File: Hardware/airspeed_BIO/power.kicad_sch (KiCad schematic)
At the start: 13 parts, among them Q1 2N7002, U1 MP2637GR-P

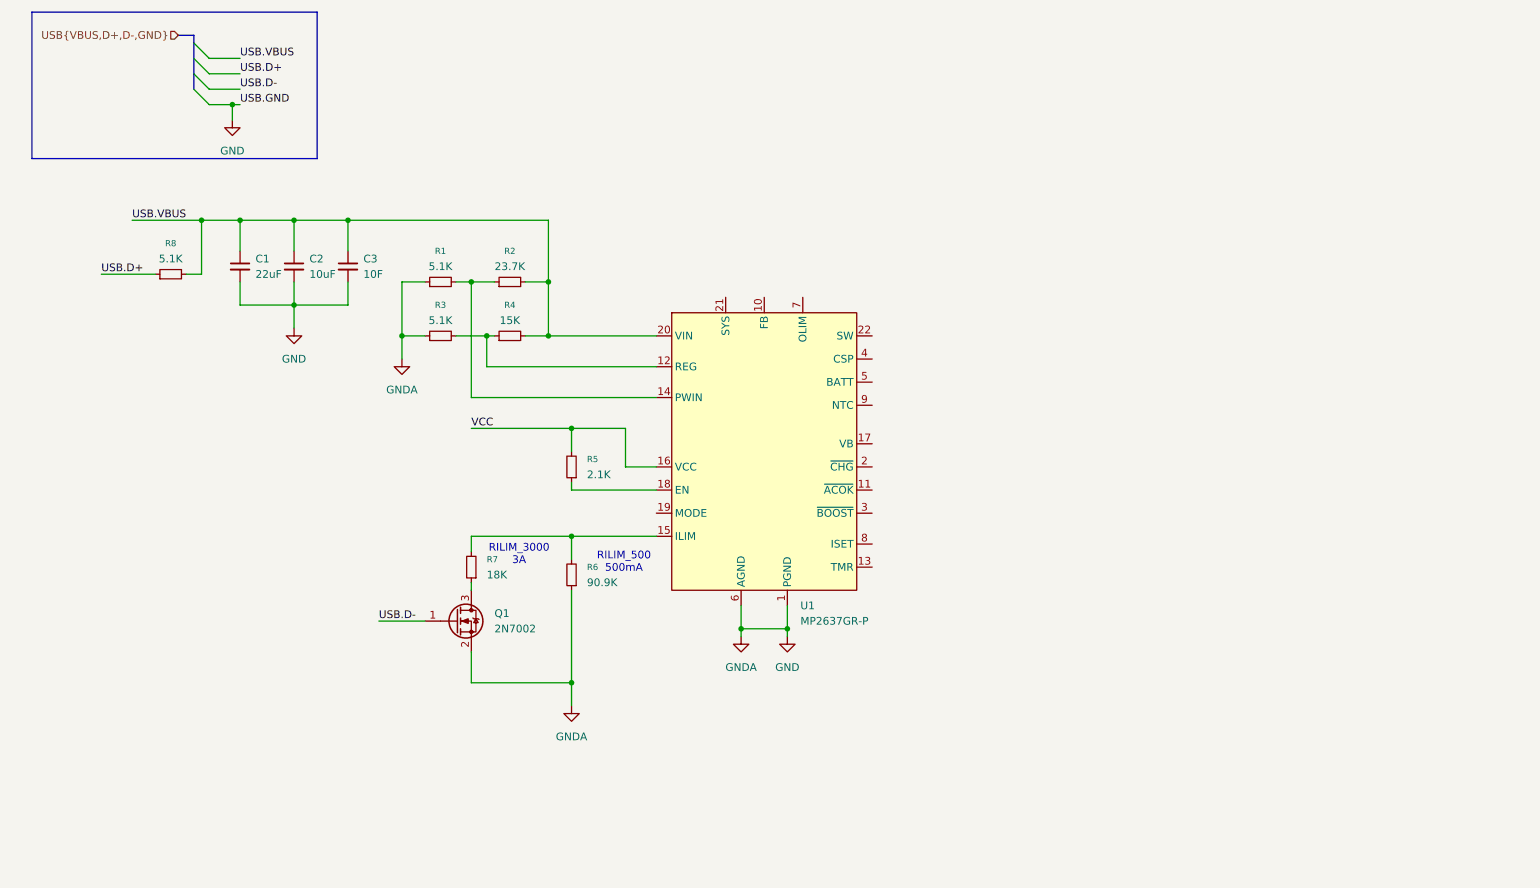
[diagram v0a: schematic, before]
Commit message: power end didn't set I limit
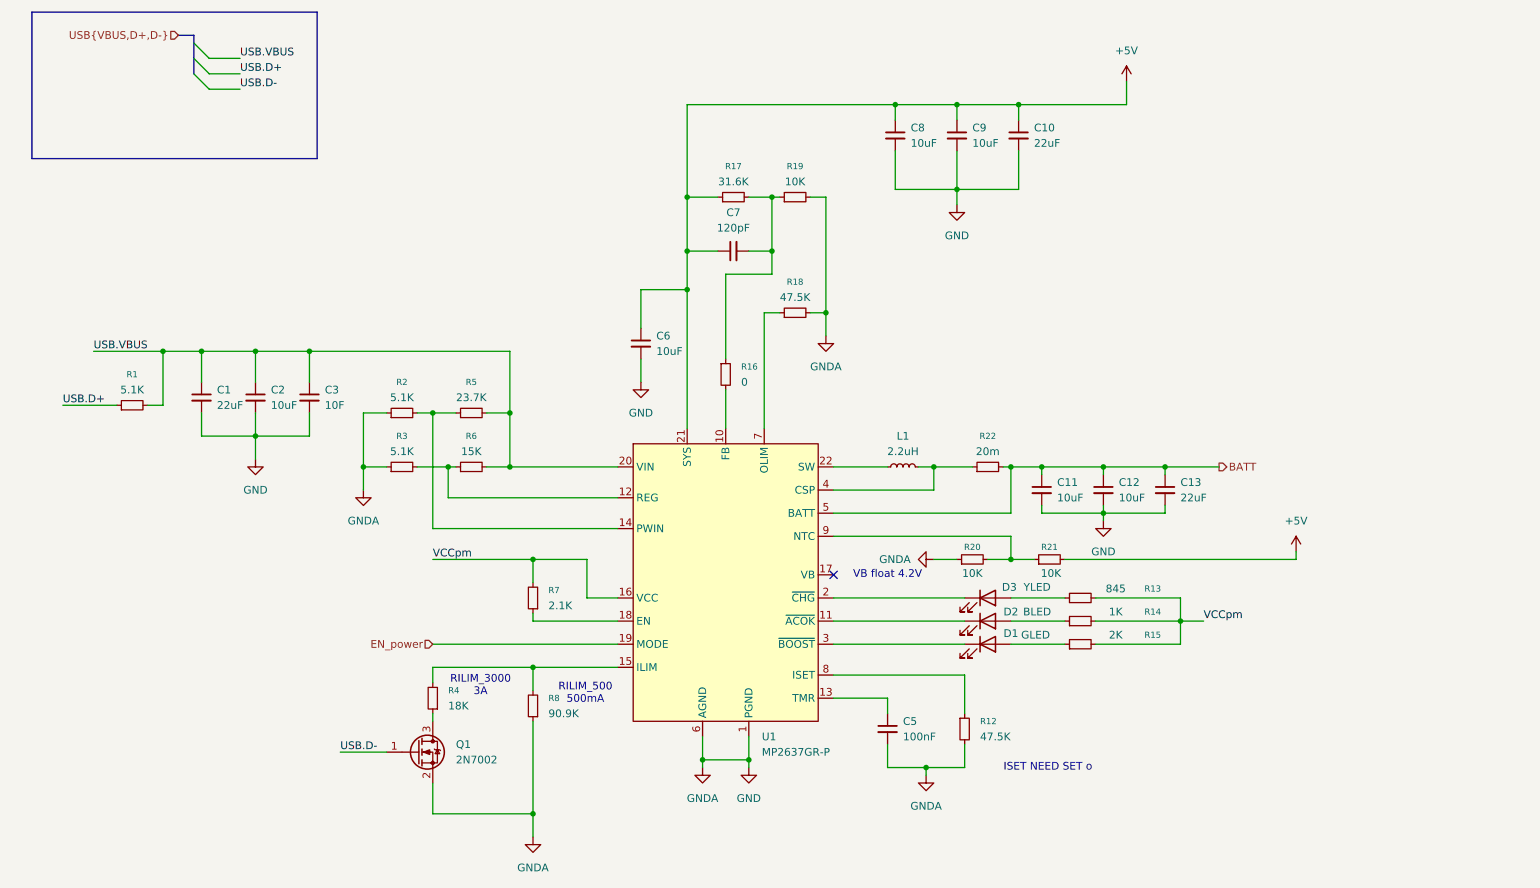
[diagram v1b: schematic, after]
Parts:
- added C10, C13: 22uF, symbol Device:C_Small
- added C11, C12, C6, C8, C9: 10uF, symbol Device:C_Small
- added C5: 100nF, symbol Device:C_Small
- added C7: 120pF, symbol Device:C_Small
- added D1: GLED, LED_SMD:LED_0603_1608Metric, symbol Device:LED
- added D2: BLED, LED_SMD:LED_0603_1608Metric, symbol Device:LED
- added D3: YLED, LED_SMD:LED_0603_1608Metric, symbol Device:LED
- added L1: 2.2uH, symbol Device:L_Small
- added R12, R18: 47.5K, symbol Device:R_Small
- added R13: 845, symbol Device:R_Small
- added R14: 1K, symbol Device:R_Small
- added R15: 2K, symbol Device:R_Small
- added R16: 0, symbol Device:R_Small
- added R17: 31.6K, symbol Device:R_Small
- added R19, R20, R21: 10K, symbol Device:R_Small
- added R22: 20m, symbol Device:R_Small
- renumbered R8 to R1, R1 to R2, R7 to R4, R2 to R5, R4 to R6, R5 to R7, R6 to R8
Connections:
- net GND: now also C10.2, C11.2, C12.2, C13.2, C5.2, C6.2, C8.2, C9.2, R12.2, R18.2, R19.2, R20.1
- net at U1.10 (FB): now also R16.2
- net at U1.11 (~{ACOK}): now also D2.1 (K)
- net at U1.13 (TMR): now also C5.1
- net EN_power: now reaches U1.19 (MODE)
- net at U1.2 (~{CHG}): now also D3.1 (K)
- net +5V: now reaches U1.21 (SYS)
- net +5V: now also C10.1, C6.1, C7.1, C8.1, C9.1, R17.1, R21.2
- net at U1.22 (SW): now also L1.1
- net at U1.3 (~{BOOST}): now also D1.1 (K)
- net at U1.4 (CSP): now also L1.2, R22.1
- net BATT: now reaches U1.5 (BATT)
- net BATT: now also C11.1, C12.1, C13.1, R22.2
- net at U1.7 (OLIM): now also R18.1
- net at U1.8 (ISET): now also R12.1
- net at U1.9 (NTC): now also R20.2, R21.1
- net VCC renamed VCCpm
- net VCCpm: now also R13.2, R14.2, R15.2
- new net: D1.2 (A), R15.1
- new net: D3.2 (A), R13.1
- new net: D2.2 (A), R14.1
- new net: C7.2, R16.1, R17.2, R19.1
- no-connect marks 0 -> 1
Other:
- note added: "ISET NEED SET o"
- note added: "VB float 4.2V"
- moved on the sheet: C1, C2, C3, Q1, R1, R2, R3, R4, R5, R6, R7, R8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

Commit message: add mcu audio
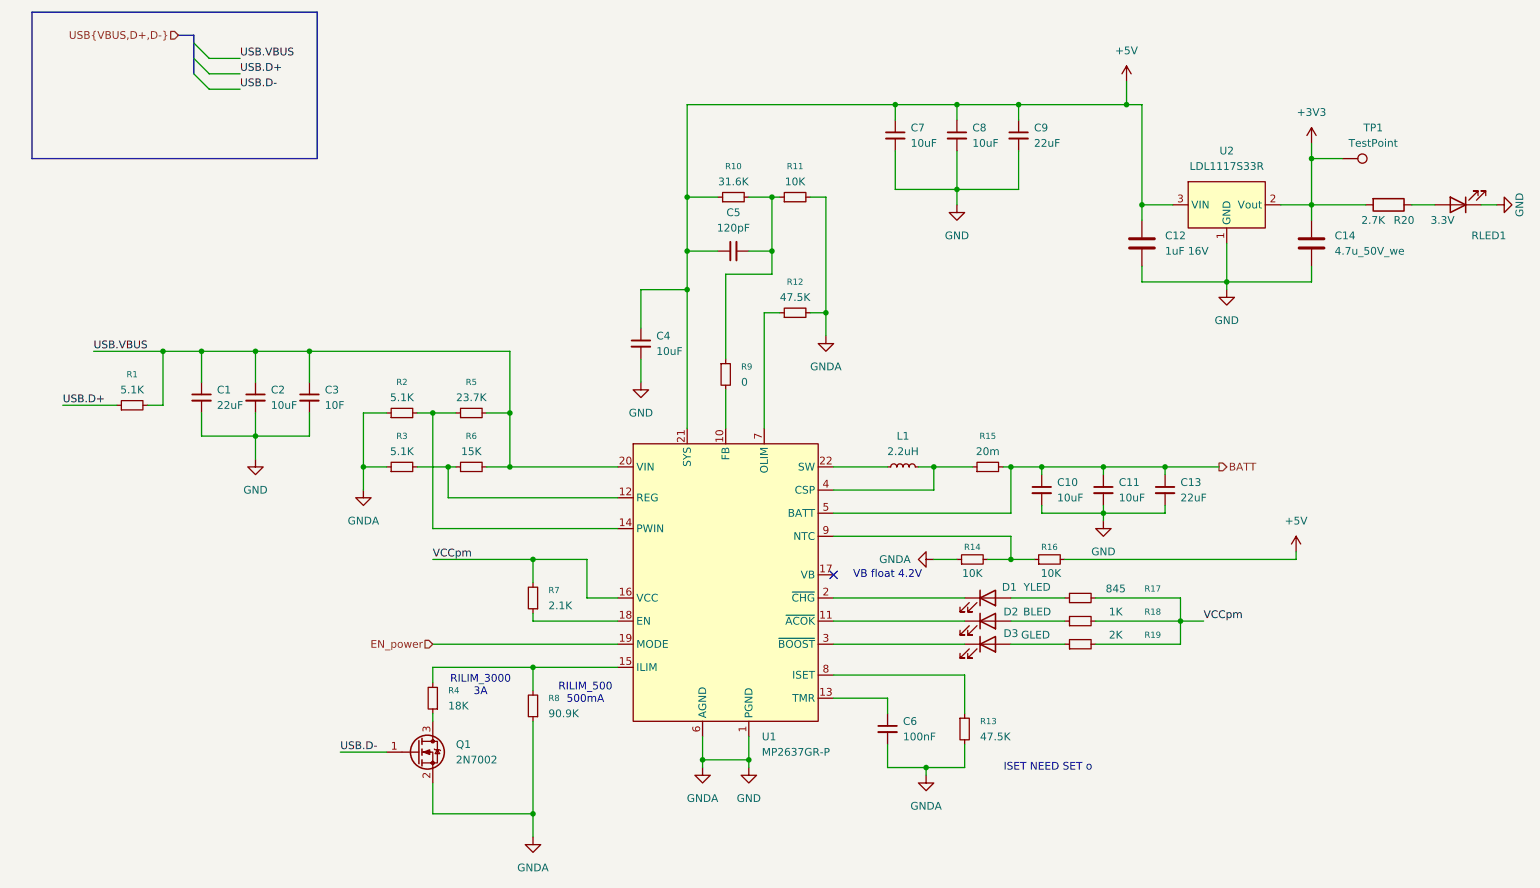
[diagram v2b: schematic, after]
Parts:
- added C12: 1uF 16V, Capacitor_SMD:C_0805_2012Metric, symbol Device:C
- added C14: 4.7u_50V_we, Capacitor_SMD:C_1210_3225Metric, symbol Device:C
- added R20: 2.7K, Resistor_SMD:R_0603_1608Metric, symbol Device:R
- added RLED1: 3.3V, LED_SMD:LED_0603_1608Metric, symbol Device:LED
- added TP1: TestPoint, TestPoint:TestPoint_THTPad_D1.0mm_Drill0.5mm, symbol Connector:TestPoint
- added U2: LDL1117S33R, Package_TO_SOT_SMD:SOT-223-3_TabPin2, symbol TTR:LDL1117S33R
- renumbered C11 to C10, C12 to C11, C6 to C4, C7 to C5, C5 to C6, C8 to C7, C9 to C8, C10 to C9, D3 to D1, D1 to D3, R17 to R10, R19 to R11, R18 to R12, R12 to R13, R20 to R14, R22 to R15, R21 to R16, R13 to R17, R14 to R18, R15 to R19, R16 to R9
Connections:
- net +5V: now also C12.1, U2.3 (VIN)
- net GND: now also C12.2, C14.2, RLED1.1 (K), U2.1 (GND)
- new net: R20.1, RLED1.2 (A)
- new net +3V3: C14.1, R20.2, TP1.1, U2.2 (Vout)
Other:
- company: (none) -> Taipei Tech Racing

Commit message: set Ilimit and set footprint
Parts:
- added TH1: 10K, Resistor_THT:R_Axial_DIN0204_L3.6mm_D1.6mm_P1.90mm_Vertical, symbol Device:Thermistor_NTC
- C1, C10, C11, C13, C2, C4, C5, C6, C7, C8, C9: footprint (none) -> Capacitor_SMD:C_0603_1608Metric
- C3: value 10F -> 10uF; footprint (none) -> Capacitor_SMD:C_0603_1608Metric
- L1: footprint (none) -> Inductor_SMD:L_1210_3225Metric; Mouser (none) -> https://www.mouser.tw/ProductDetail/Vishay-Dale/IHLP1210BZE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
- R1, R10, R11, R14, R16, R17, R2, R3, R5, R6, R7, R8, R9: footprint (none) -> Resistor_SMD:R_0603_1608Metric
- R12: value 47.5K -> 57.6K; footprint (none) -> Resistor_SMD:R_0603_1608Metric
- R13: value 47.5K -> 120K; footprint (none) -> Resistor_SMD:R_0603_1608Metric
- R15: footprint (none) -> Resistor_SMD:R_1206_3216Metric; Mouser (none) -> https://www.mouser.tw/ProductDetail/YAGEO/PE1206FRE470R02L?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
- R18: value 1K -> 1.2K; footprint (none) -> Resistor_SMD:R_0603_1608Metric
- R19: value 2K -> 2.7K; footprint (none) -> Resistor_SMD:R_0603_1608Metric
- R4: value 18K -> 45.3K; footprint (none) -> Resistor_SMD:R_0603_1608Metric
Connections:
- net GND: now also U1.23 (PGND), U1.24 (PGND), TH1.1
- net NTC: now reaches R14.2, R16.1, U1.9 (NTC)
- net NTC: now also TH1.2
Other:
- note added: "2.083A"
- note added: "R ISET 120K charge CC 1000mA 60.4K charge CC 1987mA 47.5K charge CC 2525mA"
- note added: "RILIM 1.5A"
- note added: "reserved"
- note removed: "ISET NEED SET o"
- note removed: "RILIM_3000 3A"

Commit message: layoyt end
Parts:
- removed C12: 1uF 16V, Capacitor_SMD:C_0805_2012Metric, symbol Device:C
- removed TP1: TestPoint, TestPoint:TestPoint_THTPad_D1.0mm_Drill0.5mm, symbol Connector:TestPoint
- renumbered C13 to C12, C14 to C13
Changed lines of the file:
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@@
 	)
 	(junction
-		(at 224.79 38.1)
-		(diameter 0)
-		(color 0 0 0 0)
-	)
-	(junction
 		(at 121.92 44.45)
 		(diameter 0)
@@
 	)
 	(junction
-		(at 196.85 45.72)
-		(diameter 0)
-		(color 0 0 0 0)
-	)
-	(junction
 		(at 203.2 114.3)
 		(diameter 0)
@@
 	(wire
 		(pts
-			(xy 196.85 58.42) (xy 210.82 58.42)
-		)
-		(stroke
-			(width 0)
-			(type default)
-		)
-	)
-	(wire
-		(pts
 			(xy 166.37 43.18) (xy 176.53 43.18)
 		)
@@
 	(wire
 		(pts
-			(xy 196.85 55.88) (xy 196.85 58.42)
-		)
-		(stroke
-			(width 0)
-			(type default)
-		)
-	)
-	(wire
-		(pts
 			(xy 121.92 44.45) (xy 121.92 53.34)
 		)
@@
 	(wire
 		(pts
-			(xy 224.79 38.1) (xy 224.79 45.72)
+			(xy 224.79 35.56) (xy 224.79 45.72)
 		)
 		(stroke
@@
 	(wire
 		(pts
-			(xy 224.79 35.56) (xy 224.79 38.1)
-		)
-		(stroke
-			(width 0)
-			(type default)
-		)
-	)
-	(wire
-		(pts
 			(xy 80.01 80.01) (xy 83.82 80.01)
 		)
@@
 	(wire
 		(pts
-			(xy 224.79 38.1) (xy 229.87 38.1)
-		)
-		(stroke
-			(width 0)
-			(type default)
-		)
-	)
-	(wire
-		(pts
 			(xy 50.8 83.82) (xy 59.69 83.82)
 		)
@@
 	(wire
 		(pts
-			(xy 196.85 45.72) (xy 196.85 48.26)
-		)
-		(stroke
-			(width 0)
-			(type default)
-		)
-	)
-	(wire
-		(pts
 			(xy 190.5 96.52) (xy 200.66 96.52)
 		)
@@
 	)
 	(symbol
-		(lib_id "Device:C")
-		(at 196.85 52.07 0)
-		(unit 1)
-		(exclude_from_sim no)
-		(in_bom yes)
-		(on_board yes)
-		(dnp no)
-		(fields_autoplaced yes)
-		(property "Reference" "C12"
-			(at 200.66 50.8 0)
-			(effects
-				(font
-					(size 1.27 1.27)
-				)
-				(justify left)
-			)
-		)
-		(property "Value" "1uF 16V"
-			(at 200.66 53.34 0)
-			(effects
-				(font
-					(size 1.27 1.27)
-				)
-				(justify left)
-			)
-		)
-		(property "Footprint" "Capacitor_SMD:C_0805_2012Metric"
-			(at 197.8152 55.88 0)
-			(effects
-				(font
-					(size 1.27 1.27)
-				)
-				(hide yes)
-			)
-		)
-		(property "Datasheet" "~"
-			(at 196.85 52.07 0)
-			(effects
-				(font
-					(size 1.27 1.27)
-				)
-				(hide yes)
-			)
-		)
-		(property "Description" ""
-			(at 196.85 52.07 0)
-			(effects
-				(font
-					(size 1.27 1.27)
-				)
-				(hide yes)
-			)
-		)
-		(pin "1"
-		)
-		(pin "2"
-		)
-		(instances
-			(project "airspeed_BIO"
-				(path "/6ddcf4fe-9e51-4114-8222-5fc3f810c12a/e6ebb58c-ec59-4ef0-bd77-5233a607af47"
-					(reference "C12")
-					(unit 1)
-				)
-			)
-		)
-	)
-	(symbol
 		(lib_id "Device:C_Small")
 		(at 176.53 34.29 0)
@@
 		(dnp no)
 		(fields_autoplaced yes)
-		(property "Reference" "C14"
+		(property "Reference" "C13"
 			(at 228.6 50.8 0)
 			(effects
@@
 			(project "airspeed_BIO"
 				(path "/6ddcf4fe-9e51-4114-8222-5fc3f810c12a/e6ebb58c-ec59-4ef0-bd77-5233a607af47"
-					(reference "C14")
+					(reference "C13")
 					(unit 1)
 				)
@@
 		(dnp no)
 		(fields_autoplaced yes)
-		(property "Reference" "C13"
+		(property "Reference" "C12"
 			(at 203.2 91.4462 0)
 			(effects
@@
 			(project "airspeed_BIO"
 				(path "/6ddcf4fe-9e51-4114-8222-5fc3f810c12a/e6ebb58c-ec59-4ef0-bd77-5233a607af47"
-					(reference "C13")
+					(reference "C12")
 					(unit 1)
 				)
@@
 					(unit 1)
 				)
-			)
-		)
-	)
-	(symbol
-		(lib_id "Connector:TestPoint")
-		(at 229.87 38.1 270)
-		(unit 1)
-		(exclude_from_sim no)
-		(in_bom no)
-		(on_board yes)
-		(dnp no)
-		(property "Reference" "TP1"
-			(at 234.95 33.02 90)
-			(effects
-				(font
-					(size 1.27 1.27)
-				)
-			)
-		)
-		(property "Value" "TestPoint"
-			(at 234.95 35.56 90)
-			(effects
-				(font
-					(size 1.27 1.27)
-				)
-			)
-		)
-		(property "Footprint" "TestPoint:TestPoint_THTPad_D1.0mm_Drill0.5mm"
-			(at 229.87 43.18 0)
-			(effects
-				(font
-					(size 1.27 1.27)
-				)
-				(hide yes)
-			)
-		)
-		(property "Datasheet" "~"
-			(at 229.87 43.18 0)
-			(effects
-				(font
-					(size 1.27 1.27)
-				)
-				(hide yes)
-			)
-		)
-		(property "Description" "test point"
-			(at 229.87 38.1 0)
-			(effects
-				(font
-					(size 1.27 1.27)
-				)
-				(hide yes)
-			)
-		)
-		(pin "1"
-		)
-		(instances
-			(project "airspeed_BIO"
-				(path "/6ddcf4fe-9e51-4114-8222-5fc3f810c12a/e6ebb58c-ec59-4ef0-bd77-5233a607af47"
-					(reference "TP1")
-					(unit 1)
-				)
